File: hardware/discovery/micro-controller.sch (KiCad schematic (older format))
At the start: 0 parts

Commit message: Discovery: add the MCU
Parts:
- added U?: STM32F407VG, TQFP100, symbol STM32F407VG
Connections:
- new net Audio_Reset: U?.85 (PD4/FSMC_NOE/USART2_RTS/EVENTOUT)
- new net Audio_SCL: U?.92 (PB6/I2C1_SCL/TIM4_CH1/CAN2_TX/DCMI_D5/USART1_TX/EVENTOUT)
- new net Audio_SDA: U?.96 (PB9/SPI2_NSS/I2S2_WS/TIM4_CH4/TIM11_CH1/SDIO_D5/DCMI_D7/I2C1_SDA/CAN1_TX/EVENTOUT)
- new net B1: U?.9 (PC15/OSC32_OUT/EVENTOUT)
- new net B10: U?.8 (PC14/OSC32_IN/EVENTOUT)
- new net B11: U?.5 (PE6/TRACED3_/_FSMC_A22/TIM9_CH2/DCMI_D7/EVENTOUT)
- new net B12: U?.4 (PE5/TRACED2/FSMC_A21/TIM9_CH1/DCMI_D6/EVENTOUT)
- new net B13: U?.1 (PE2/TRACECLK/FSMC_A23/ETH_MII_TXD3/EVENTOUT)
- new net B14: U?.90 (PB4/NJTRST/SPI3_MISO/TIM3_CH1/SPI1_MISO/I2S3ext_SD/EVENTOUT)
- new net B15: U?.89 (PB3/JTDO/TRACESWO/SPI3_SCK/I2S3_CK/TIM2_CH2/SPI1_SCK/EVENTOUT)
- new net B16: U?.84 (PD3/FSMC_CLK/USART2_CTS/EVENTOUT)
- new net B2: U?.7 (PC13/EVENTOUT)
- new net B3: U?.3 (PE4/TRACED1/FSMC_A20/DCMI_D4/EVENTOUT)
- new net B4: U?.95 (PB8/TIM4_CH3/SDIO_D4/TIM10_CH1/DCMI_D6/ETH_MII_TXD3/I2C1_SCL/CAN1_RX/EVENTOUT)
- new net B5: U?.91 (PB5/I2C1_SMBA/CAN2_RX/OTG_HS_ULPI_D7/ETH_PPS_OUT/TIM3_CH2/SPI1_MOSI/SPI3_MOSI/DCMI_D10/I2S3_SD/EVENTOUT)
- new net B6: U?.88 (PD7/USART2_CK/FSMC_NE1/FSMC_NCE2/EVENTOUT)
- new net B7: U?.87 (PD6/FSMC_NWAIT/USART2_RX/EVENTOUT)
- new net B8: U?.82 (PD1/FSMC_D3/CAN1_TX/EVENTOUT)
- new net B9: U?.93 (PB7/I2C1_SDA/FSMC_NL/DCMI_VSYNC/USART1_RX/TIM4_CH2/EVENTOUT)
- new net BF1: U?.16 (PC1/ETH_MDC/_EVENTOUT)
- new net BF2: U?.17 (PC2/SPI2_MISO/OTG_HS_ULPI_DIR/ETH_MII_TXD2/I2S2ext_SD/EVENTOUT)
- new net BF3: U?.55 (PD8/FSMC_D13/USART3_TX/EVENTOUT)
- new net BF4: U?.54 (PB15/SPI2_MOSI/I2S2_SD/TIM1_CH3N/TIM8_CH3N/TIM12_CH2/OTG_HS_DP/EVENTOUT)
- new net BF5: U?.57 (PD10/FSMC_D15/USART3_CK/EVENTOUT)
- new net BPM_VOL: U?.56 (PD9/FSMC_D14/USART3_RX/EVENTOUT)
- new net COL1: U?.63 (PC6/I2S2_MCK/TIM8_CH1/SDIO_D6/USART6_TX/DCMI_D0/TIM3_CH1/EVENTOUT)
- new net COL2: U?.69 (PA10/USART1_RX/TIM1_CH3/OTG_FS_ID/DCMI_D1/EVENTOUT)
- new net COL3: U?.25 (PA2/USART2_TX/TIM5_CH3/TIM9_CH1/TIM2_CH3/ETH_MDIO/EVENTOUT)
- new net COL4: U?.18 (PC3/SPI2_MOSI/I2S2_SD/OTG_HS_ULPI_NXT/ETH_MII_TX_CLK/EVENTOUT)
- new net COL5: U?.15 (PC0/OTG_HS_ULPI_STP/EVENTOUT)
- new net FX: U?.58 (PD11/FSMC_CLE/FSMC_A16/USART3_CTS/EVENTOUT)
- new net I2S3_MCK: U?.64 (PC7/I2S3_MCK/TIM8_CH2/SDIO_D7/USART6_RX/DCMI_D1/TIM3_CH2/EVENTOUT)
- new net I2S3_SCK: U?.78 (PC10/SPI3_SCK/I2S3_CK/UART4_TX/SDIO_D2/DCMI_D8/USART3_TX/EVENTOUT)
- new net I2S3_SD: U?.80 (PC12/UART5_TX/SDIO_CK/DCMI_D9/SPI3_MOSI/I2S3_SD/USART3_CK/EVENTOUT)
- new net I2S3_WS: U?.29 (PA4/SPI1_NSS/SPI3_NSS/USART2_CK/DCMI_HSYNC/OTG_HS_SOF/I2S3_WS/EVENTOUT)
- new net POT1: U?.24 (PA1/USART2_RTS/UART4_RX/ETH_RMII_REF_CLK/ETH_MII_RX_CLK/TIM5_CH2/TIMM2_CH2/EVENTOUT)
- new net POT2: U?.26 (PA3/USART2_RX/TIM5_CH4/TIM9_CH2/TIM2_CH4/OTG_HS_ULPI_D0/ETH_MII_COL/EVENTOUT)
- new net Play: U?.81 (PD0/FSMC_D2/CAN1_RX/EVENTOUT)
- new net ROW1: U?.66 (PC9/I2S_CKIN/MCO2/TIM8_CH4/SDIO_D1/I2C3_SDA/DCMI_D3/TIM3_CH4/EVENTOUT)
- new net ROW2: U?.65 (PC8/TIM8_CH3/SDIO_D0/TIM3_CH3/USART6_CK/DCMI_D2/EVENTOUT)
- new net ROW3: U?.77 (PA15/JTDI/SPI3_NSS/I2S3_WS/TIM2_CH1_ETR/SPI1_NSS/EVENTOUT)
- new net ROW4: U?.79 (PC11/UART4_RX/SPI3_MISO/SDIO_D3/DCMI_D4/USART3_RX/I2S3ext_SD/EVENTOUT)
- new net ROw5: U?.67 (PA8/MCO1/USART1_CK/TIM1_CH1/I2C3_SCL/OTG_FS_SOF/EVENTOUT)
- new net SPI1_MISO: U?.31 (PA6/SPI1_MISO/TIM8_BKIN/TIM13_CH1/DCMI_PIXCLK/TIM3_CH1/TIM1_BKIN/EVENTOUT)
- new net SPI1_MOSI: U?.32 (PA7/SPI1_MOSI/TIM8_CH1N/TIM14_CH1/TIM3_CH2/ETH_MII_RX_DV/TIM1_CH1N/RMII_CRS_DV/EVENTOUT)
- new net SPI1_SCK: U?.30 (PA5/SPI1_SCK/OTG_HS_ULPI_CK/TIM2_CH1_ETR/TIM8_CHIN/EVENTOUT)
- new net SWCLK: U?.76 (PA14/JTCK/SWCLK/EVENTOUT)
- new net SWDIO: U?.72 (PA13/JTMS/SWDIO/EVENTOUT)
- new net USB_Over_Current: U?.86 (PD5/FSMC_NWE/USART2_TX/EVENTOUT)
- new net VBUS: U?.68 (PA9/USART1_TX/TIM1_CH2/I2C3_SMBA/DCMI_D0/EVENTOUT)
- new net Write: U?.83 (PD2/TIM3_ETR/UART5_RX/SDIO_CMD/DCMI_D11/EVENTOUT)
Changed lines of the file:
@@
 EELAYER 25 0
 EELAYER END
-$Descr A4 11693 8268
+$Descr A3 16535 11693
 encoding utf-8
 Sheet 3 3
@@
 Comment4 ""
 $EndDescr
+$Comp
+L STM32F407VG U?
+U 1 1 585DBF7E
+P 7850 4850
+F 0 "U?" H 7850 4850 60  0000 C CNN
+F 1 "STM32F407VG" H 7850 4950 60  0000 C CNN
+F 2 "TQFP100" H 7850 4750 60  0000 C CNN
+F 3 "" H 7850 4850 60  0001 C CNN
+	1    7850 4850
+	1    0    0    -1
+$EndComp
+Text GLabel 2850 4200 0    60   Input ~ 0
+POT1
+Text GLabel 2850 4300 0    60   Input ~ 0
+COL3
+Text GLabel 2850 4400 0    60   Input ~ 0
+POT2
+Text GLabel 2850 4500 0    60   Input ~ 0
+I2S3_WS
+Text GLabel 2850 4600 0    60   Input ~ 0
+SPI1_SCK
+Text GLabel 2850 4700 0    60   Input ~ 0
+SPI1_MISO
+Text GLabel 2850 4800 0    60   Input ~ 0
+SPI1_MOSI
+Text GLabel 2850 4900 0    60   Input ~ 0
+ROw5
+Text GLabel 2850 5000 0    60   Input ~ 0
+VBUS
+Text GLabel 2850 5100 0    60   Input ~ 0
+COL2
+Text GLabel 2850 5400 0    60   Input ~ 0
+SWDIO
+Text GLabel 2850 5500 0    60   Input ~ 0
+SWCLK
+Text GLabel 2850 5600 0    60   Input ~ 0
+ROW3
+Text GLabel 2850 6200 0    60   Input ~ 0
+B15
+Text GLabel 2850 6300 0    60   Input ~ 0
+B14
+Text GLabel 2850 6400 0    60   Input ~ 0
+B5
+Text GLabel 2850 6500 0    60   Input ~ 0
+Audio_SCL
+Text GLabel 2850 6600 0    60   Input ~ 0
+B9
+Text GLabel 2850 6700 0    60   Input ~ 0
+B4
+Text GLabel 2850 6800 0    60   Input ~ 0
+Audio_SDA
+Text GLabel 2850 7400 0    60   Input ~ 0
+BF4
+Text GLabel 12850 5900 2    60   Input ~ 0
+COL5
+Text GLabel 12850 6000 2    60   Input ~ 0
+BF1
+Text GLabel 12850 6100 2    60   Input ~ 0
+BF2
+Text GLabel 12850 6200 2    60   Input ~ 0
+COL4
+Text GLabel 12850 6500 2    60   Input ~ 0
+COL1
+Text GLabel 12850 6600 2    60   Input ~ 0
+I2S3_MCK
+Text GLabel 12850 6700 2    60   Input ~ 0
+ROW2
+Text GLabel 12850 6800 2    60   Input ~ 0
+ROW1
+Text GLabel 12850 6900 2    60   Input ~ 0
+I2S3_SCK
+Text GLabel 12850 7000 2    60   Input ~ 0
+ROW4
+Text GLabel 12850 7100 2    60   Input ~ 0
+I2S3_SD
+Text GLabel 12850 7200 2    60   Input ~ 0
+B2
+Text GLabel 12850 7300 2    60   Input ~ 0
+B10
+Text GLabel 12850 7400 2    60   Input ~ 0
+B1
+Text GLabel 12850 4100 2    60   Input ~ 0
+Play
+Text GLabel 12850 4200 2    60   Input ~ 0
+B8
+Text GLabel 12850 4300 2    60   Input ~ 0
+Write
+Text GLabel 12850 4400 2    60   Input ~ 0
+B16
+Text GLabel 12850 4500 2    60   Input ~ 0
+Audio_Reset
+Text GLabel 12850 4600 2    60   Input ~ 0
+USB_Over_Current
+Text GLabel 12850 4700 2    60   Input ~ 0
+B7
+Text GLabel 12850 4800 2    60   Input ~ 0
+B6
+Text GLabel 12850 4900 2    60   Input ~ 0
+BF3
+Text GLabel 12850 5000 2    60   Input ~ 0
+BPM_VOL
+Text GLabel 12850 5100 2    60   Input ~ 0
+BF5
+Text GLabel 12850 5200 2    60   Input ~ 0
+FX
+Text GLabel 12850 2500 2    60   Input ~ 0
+B13
+Text GLabel 12850 2700 2    60   Input ~ 0
+B3
+Text GLabel 12850 2800 2    60   Input ~ 0
+B12
+Text GLabel 12850 2900 2    60   Input ~ 0
+B11
 $EndSCHEMATC

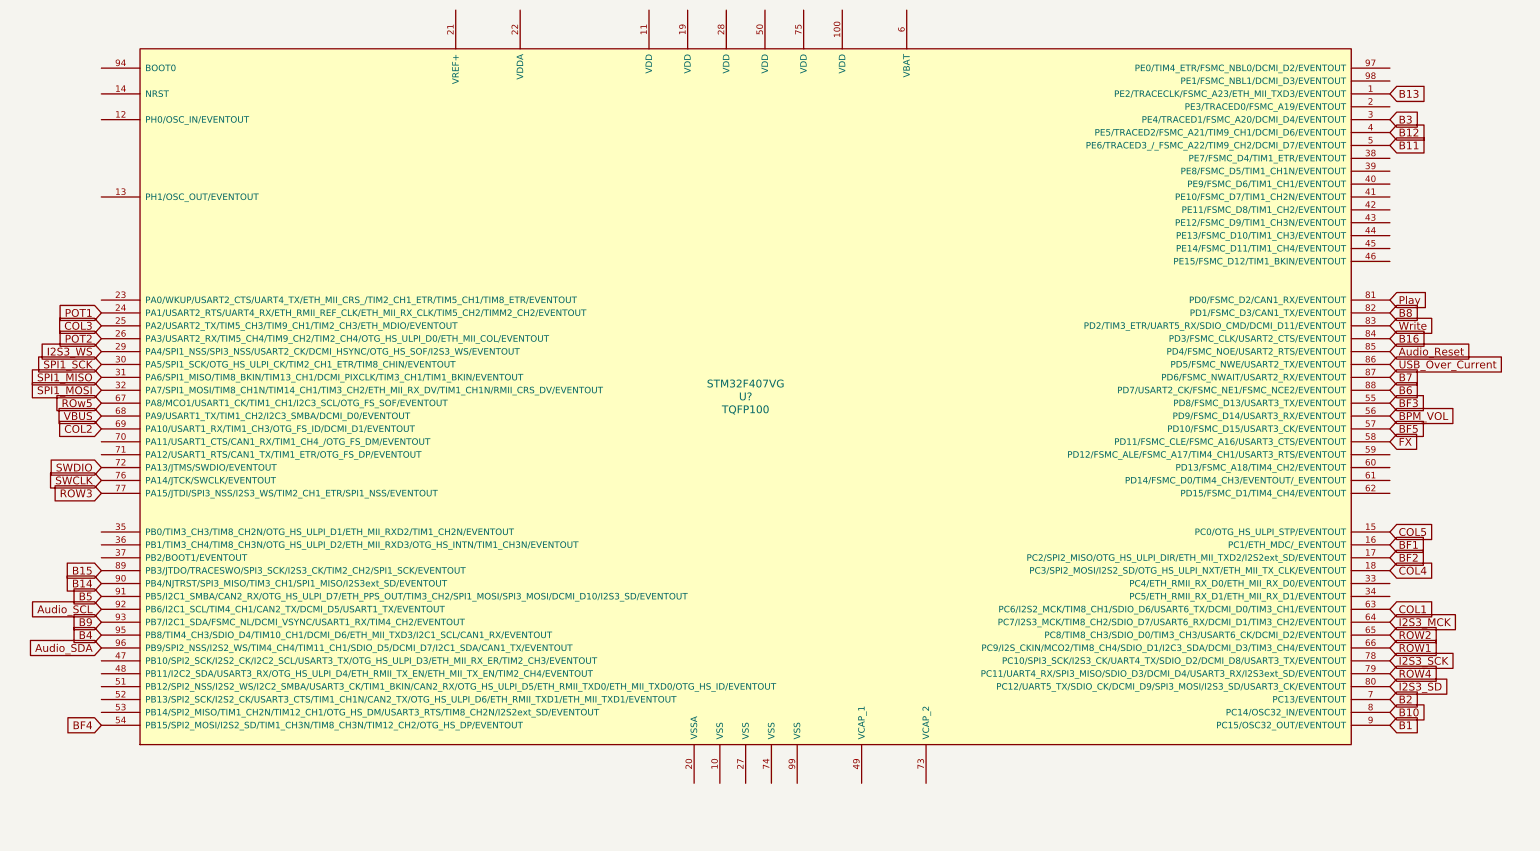
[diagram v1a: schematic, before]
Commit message: Discovery: Fix channel button labels
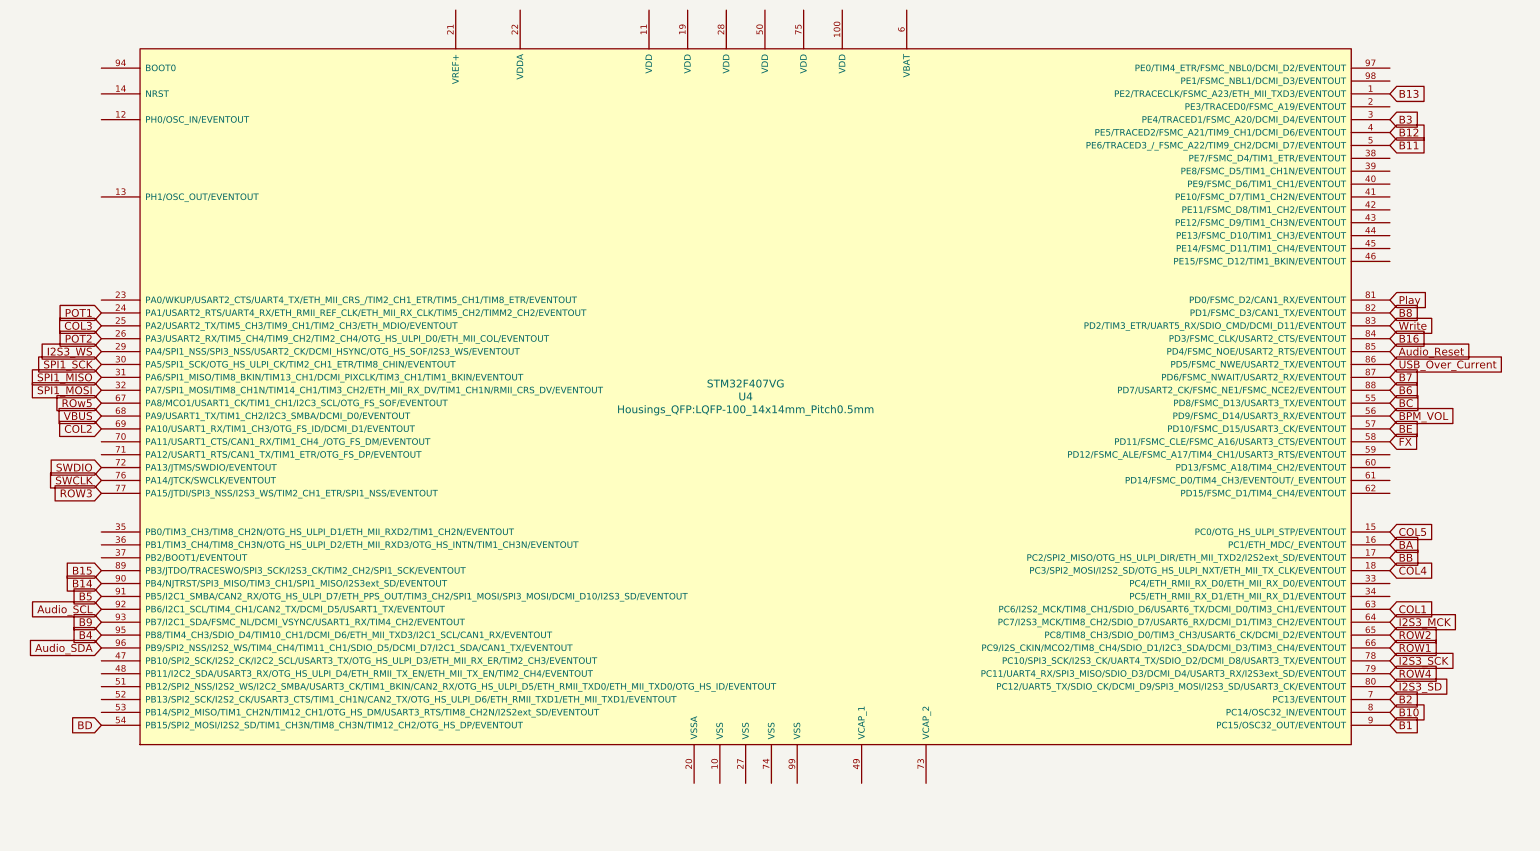
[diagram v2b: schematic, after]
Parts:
- U4: renamed from U?; footprint TQFP100 -> Housings_QFP:LQFP-100_14x14mm_Pitch0.5mm
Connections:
- net BF1 renamed BA
- net BF2 renamed BB
- net BF3 renamed BC
- net BF4 renamed BD
- net BF5 renamed BE
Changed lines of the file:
@@
 $EndDescr
 $Comp
-L STM32F407VG U?
+L STM32F407VG U4
 U 1 1 585DBF7E
 P 7850 4850
-F 0 "U?" H 7850 4850 60  0000 C CNN
+F 0 "U4" H 7850 4850 60  0000 C CNN
 F 1 "STM32F407VG" H 7850 4950 60  0000 C CNN
-F 2 "TQFP100" H 7850 4750 60  0000 C CNN
+F 2 "Housings_QFP:LQFP-100_14x14mm_Pitch0.5mm" H 7850 4750 60  0000 C CNN
 F 3 "" H 7850 4850 60  0001 C CNN
 	1    7850 4850
@@
 Audio_SDA
 Text GLabel 2850 7400 0    60   Input ~ 0
-BF4
+BD
 Text GLabel 12850 5900 2    60   Input ~ 0
 COL5
 Text GLabel 12850 6000 2    60   Input ~ 0
-BF1
+BA
 Text GLabel 12850 6100 2    60   Input ~ 0
-BF2
+BB
 Text GLabel 12850 6200 2    60   Input ~ 0
 COL4
@@
 B6
 Text GLabel 12850 4900 2    60   Input ~ 0
-BF3
+BC
 Text GLabel 12850 5000 2    60   Input ~ 0
 BPM_VOL
 Text GLabel 12850 5100 2    60   Input ~ 0
-BF5
+BE
 Text GLabel 12850 5200 2    60   Input ~ 0
 FX

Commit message: Discovery start power section
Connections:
- net FS_DM: now reaches U4.70 (PA11/USART1_CTS/CAN1_RX/TIM1_CH4_/OTG_FS_DM/EVENTOUT)
- net FS_DP: now reaches U4.71 (PA12/USART1_RTS/CAN1_TX/TIM1_ETR/OTG_FS_DP/EVENTOUT)
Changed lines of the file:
@@
 LIBS:contrib
 LIBS:valves
-LIBS:w_connectors
 LIBS:stm32f4_disco_header
 LIBS:74xgxx
@@
 Text GLabel 12850 2900 2    60   Input ~ 0
 B11
+Text GLabel 2850 5200 0    60   Input ~ 0
+FS_DM
+Text GLabel 2850 5300 0    60   Input ~ 0
+FS_DP
 $EndSCHEMATC

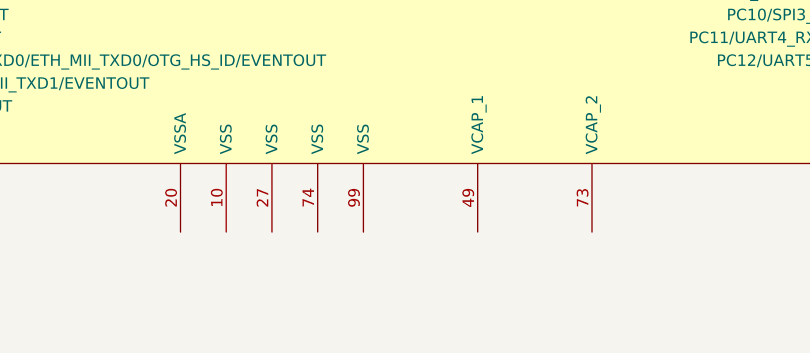
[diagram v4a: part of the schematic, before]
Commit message: Discovery: SMT2F4 grounding
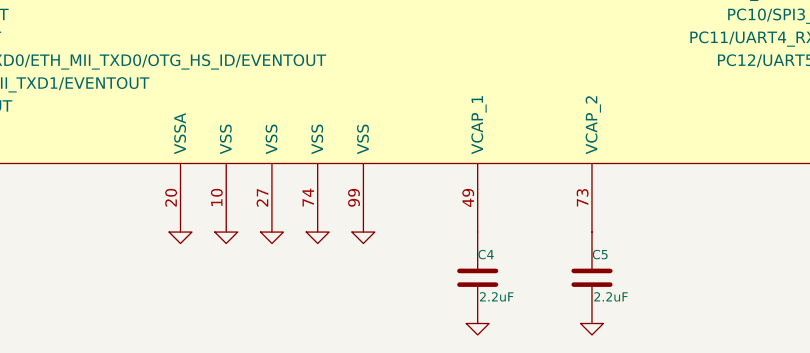
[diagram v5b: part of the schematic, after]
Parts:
- added C4, C5: 2.2uF, Capacitors_SMD:C_0805, symbol C
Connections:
- net GND: now reaches U4.10 (VSS)
- net GND: now also U4.20 (VSSA), U4.27 (VSS), U4.74 (VSS), U4.99 (VSS), C4.2, C5.2
- net at U4.49 (VCAP_1): now also C4.1
- net at U4.73 (VCAP_2): now also C5.1
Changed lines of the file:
@@
 Text GLabel 2850 5300 0    60   Input ~ 0
 FS_DP
+$Comp
+L GND #PWR016
+U 1 1 585E3358
+P 7650 7850
+F 0 "#PWR016" H 7650 7850 30  0001 C CNN
+F 1 "GND" H 7650 7780 30  0001 C CNN
+F 2 "" H 7650 7850 60  0001 C CNN
+F 3 "" H 7650 7850 60  0001 C CNN
+	1    7650 7850
+	1    0    0    -1
+$EndComp
+$Comp
+L GND #PWR017
+U 1 1 585E336D
+P 7850 7850
+F 0 "#PWR017" H 7850 7850 30  0001 C CNN
+F 1 "GND" H 7850 7780 30  0001 C CNN
+F 2 "" H 7850 7850 60  0001 C CNN
+F 3 "" H 7850 7850 60  0001 C CNN
+	1    7850 7850
+	1    0    0    -1
+$EndComp
+$Comp
+L GND #PWR018
+U 1 1 585E337B
+P 8050 7850
+F 0 "#PWR018" H 8050 7850 30  0001 C CNN
+F 1 "GND" H 8050 7780 30  0001 C CNN
+F 2 "" H 8050 7850 60  0001 C CNN
+F 3 "" H 8050 7850 60  0001 C CNN
+	1    8050 7850
+	1    0    0    -1
+$EndComp
+$Comp
+L GND #PWR019
+U 1 1 585E3389
+P 8250 7850
+F 0 "#PWR019" H 8250 7850 30  0001 C CNN
+F 1 "GND" H 8250 7780 30  0001 C CNN
+F 2 "" H 8250 7850 60  0001 C CNN
+F 3 "" H 8250 7850 60  0001 C CNN
+	1    8250 7850
+	1    0    0    -1
+$EndComp
+$Comp
+L GND #PWR020
+U 1 1 585E3397
+P 7450 7850
+F 0 "#PWR020" H 7450 7850 30  0001 C CNN
+F 1 "GND" H 7450 7780 30  0001 C CNN
+F 2 "" H 7450 7850 60  0001 C CNN
+F 3 "" H 7450 7850 60  0001 C CNN
+	1    7450 7850
+	1    0    0    -1
+$EndComp
+$Comp
+L C C4
+U 1 1 585E3587
+P 8750 8050
+F 0 "C4" H 8750 8150 40  0000 L CNN
+F 1 "2.2uF" H 8756 7965 40  0000 L CNN
+F 2 "Capacitors_SMD:C_0805" H 8788 7900 30  0001 C CNN
+F 3 "" H 8750 8050 60  0000 C CNN
+	1    8750 8050
+	1    0    0    -1
+$EndComp
+$Comp
+L C C5
+U 1 1 585E35B8
+P 9250 8050
+F 0 "C5" H 9250 8150 40  0000 L CNN
+F 1 "2.2uF" H 9256 7965 40  0000 L CNN
+F 2 "Capacitors_SMD:C_0805" H 9288 7900 30  0001 C CNN
+F 3 "" H 9250 8050 60  0000 C CNN
+	1    9250 8050
+	1    0    0    -1
+$EndComp
+$Comp
+L GND #PWR021
+U 1 1 585E35DF
+P 8750 8250
+F 0 "#PWR021" H 8750 8250 30  0001 C CNN
+F 1 "GND" H 8750 8180 30  0001 C CNN
+F 2 "" H 8750 8250 60  0001 C CNN
+F 3 "" H 8750 8250 60  0001 C CNN
+	1    8750 8250
+	1    0    0    -1
+$EndComp
+$Comp
+L GND #PWR022
+U 1 1 585E35F3
+P 9250 8250
+F 0 "#PWR022" H 9250 8250 30  0001 C CNN
+F 1 "GND" H 9250 8180 30  0001 C CNN
+F 2 "" H 9250 8250 60  0001 C CNN
+F 3 "" H 9250 8250 60  0001 C CNN
+	1    9250 8250
+	1    0    0    -1
+$EndComp
 $EndSCHEMATC
